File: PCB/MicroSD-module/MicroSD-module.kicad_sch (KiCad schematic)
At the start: 12 parts, among them J1 Connector, K1 HYC77-TF09-200, U1 SE5218, U2 TXB0104PWR

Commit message: More OCD
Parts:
- renumbered C3 to C2, C2 to C3
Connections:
- net GND: now also K1.SHIELD
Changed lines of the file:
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@@
+		)
+	)
+	(global_label "GND"
+		(shape input)
+		(at 106.68 36.83 270)
+		(fields_autoplaced yes)
+		(effects
+			(font
+				(size 1.27 1.27)
+			)
+			(justify right)
+		)
+		(property "Intersheetrefs" "${INTERSHEET_REFS}"
+			(at 106.68 43.6857 90)
+			(effects
+				(font
+					(size 1.27 1.27)
+				)
+				(justify right)
+				(hide yes)
+			)
 		)
 	)
@@
 		(on_board yes)
 		(dnp no)
-		(property "Reference" "C2"
+		(property "Reference" "C3"
 			(at 137.16 34.29 0)
 			(effects
@@
 			(project "Small"
 				(path "/596d0583-1d97-453e-b84c-75eed809afa2"
-					(reference "C2")
+					(reference "C3")
 					(unit 1)
 				)
@@
 		(pin "8"
 		)
+		(pin "SHIELD"
+		)
 		(instances
 			(project "Small"
@@
 		(on_board yes)
 		(dnp no)
-		(property "Reference" "C3"
+		(property "Reference" "C2"
 			(at 66.04 102.87 90)
 			(effects
@@
 			(project "Small"
 				(path "/596d0583-1d97-453e-b84c-75eed809afa2"
-					(reference "C3")
+					(reference "C2")
 					(unit 1)
 				)

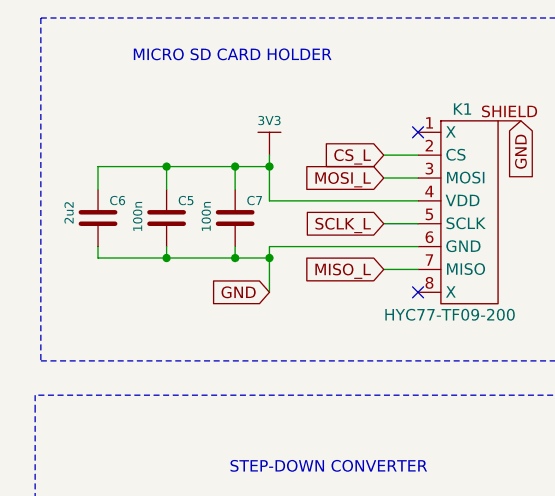
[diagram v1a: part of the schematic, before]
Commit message: Fix microSD caps
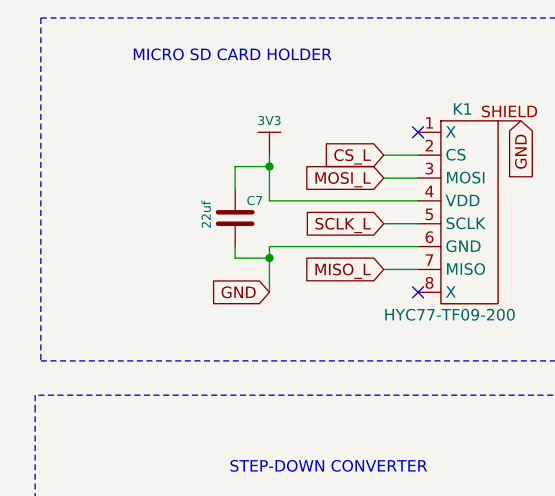
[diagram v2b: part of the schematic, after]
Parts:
- removed C5: 100n, Capacitor_SMD:C_0603_1608Metric, symbol e-radionica.com schematics:0603C
- removed C6: 2u2, Capacitor_SMD:C_0603_1608Metric, symbol e-radionica.com schematics:0603C
- C7: value 100n -> 22uf; footprint Capacitor_SMD:C_0603_1608Metric -> Capacitor_SMD:C_0805_2012Metric; LCSC C1590 -> C45783

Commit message: OCD
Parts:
- renumbered C7 to C5
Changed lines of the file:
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@@
 		(on_board yes)
 		(dnp no)
-		(property "Reference" "C7"
+		(property "Reference" "C5"
 			(at 76.2 45.72 90)
 			(effects
@@
 			(project "Small"
 				(path "/596d0583-1d97-453e-b84c-75eed809afa2"
-					(reference "C7")
+					(reference "C5")
 					(unit 1)
 				)

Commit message: Update details
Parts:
- U1: value SE5218 -> SE5218ALG-LF
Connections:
- net CS: now also U2.10 (B4); no longer U2.13 (B1)
- net CS_L: now also U2.5 (A4); no longer U2.2 (A1)
- net MISO: now also U2.13 (B1); no longer U2.10 (B4)
- net MISO_L: now also U2.2 (A1); no longer U2.5 (A4)
- net MOSI: now also U2.11 (B3); no longer U2.12 (B2)
- net MOSI_L: now also U2.4 (A3); no longer U2.3 (A2)
- net SCK: now also U2.12 (B2); no longer U2.11 (B3)
- net SCLK_L: now also U2.3 (A2); no longer U2.4 (A3)
